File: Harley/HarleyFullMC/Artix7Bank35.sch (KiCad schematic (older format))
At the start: 11 parts, among them U1 xc7a50tcsg324pkg

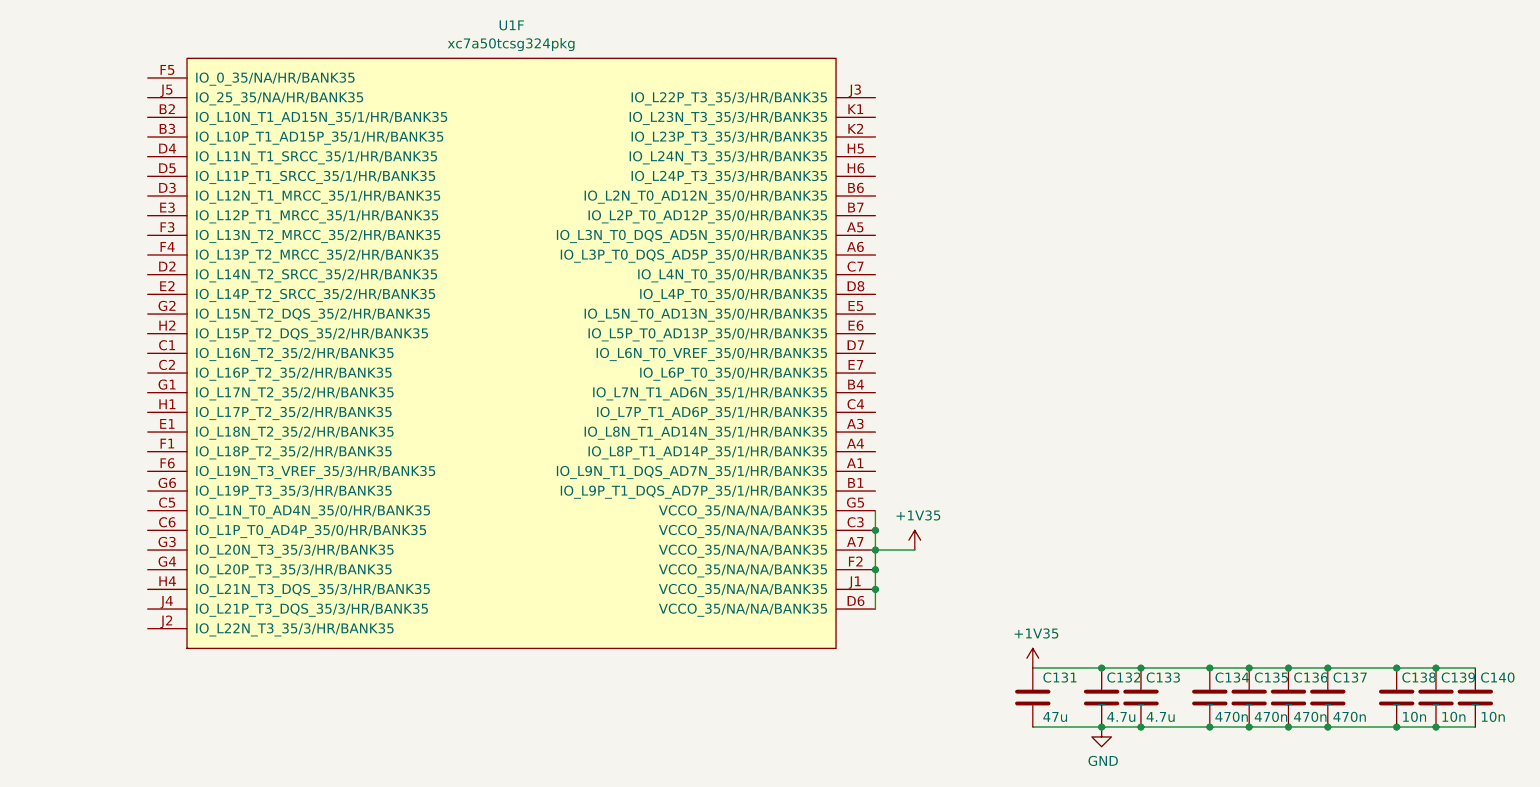
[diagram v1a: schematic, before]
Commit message: finished placement and started routing
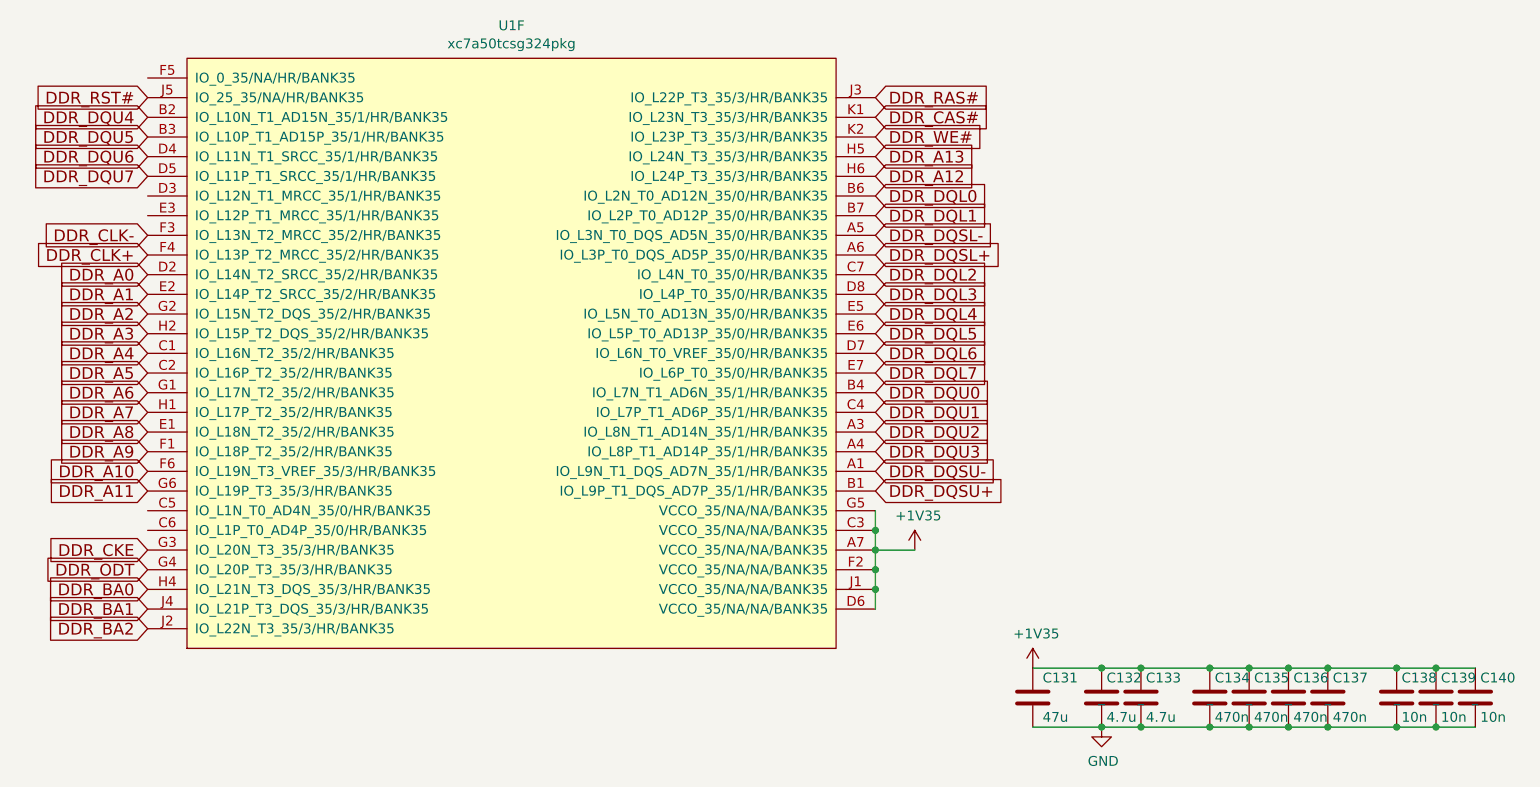
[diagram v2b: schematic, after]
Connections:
- net DDR_DQSU-: now reaches U1.A1 (IO_L9N_T1_DQS_AD7N_35/1/HR/BANK35)
- net DDR_DQU2: now reaches U1.A3 (IO_L8N_T1_AD14N_35/1/HR/BANK35)
- net DDR_DQU3: now reaches U1.A4 (IO_L8P_T1_AD14P_35/1/HR/BANK35)
- net DDR_DQSL-: now reaches U1.A5 (IO_L3N_T0_DQS_AD5N_35/0/HR/BANK35)
- net DDR_DQSL+: now reaches U1.A6 (IO_L3P_T0_DQS_AD5P_35/0/HR/BANK35)
- net DDR_DQSU+: now reaches U1.B1 (IO_L9P_T1_DQS_AD7P_35/1/HR/BANK35)
- net DDR_DQU4: now reaches U1.B2 (IO_L10N_T1_AD15N_35/1/HR/BANK35)
- net DDR_DQU5: now reaches U1.B3 (IO_L10P_T1_AD15P_35/1/HR/BANK35)
- net DDR_DQU0: now reaches U1.B4 (IO_L7N_T1_AD6N_35/1/HR/BANK35)
- net DDR_DQL0: now reaches U1.B6 (IO_L2N_T0_AD12N_35/0/HR/BANK35)
- net DDR_DQL1: now reaches U1.B7 (IO_L2P_T0_AD12P_35/0/HR/BANK35)
- net DDR_A4: now reaches U1.C1 (IO_L16N_T2_35/2/HR/BANK35)
- net DDR_A5: now reaches U1.C2 (IO_L16P_T2_35/2/HR/BANK35)
- net DDR_DQU1: now reaches U1.C4 (IO_L7P_T1_AD6P_35/1/HR/BANK35)
- net DDR_DQL2: now reaches U1.C7 (IO_L4N_T0_35/0/HR/BANK35)
- net DDR_A0: now reaches U1.D2 (IO_L14N_T2_SRCC_35/2/HR/BANK35)
- net DDR_DQU6: now reaches U1.D4 (IO_L11N_T1_SRCC_35/1/HR/BANK35)
- net DDR_DQU7: now reaches U1.D5 (IO_L11P_T1_SRCC_35/1/HR/BANK35)
- net DDR_DQL6: now reaches U1.D7 (IO_L6N_T0_VREF_35/0/HR/BANK35)
- net DDR_DQL3: now reaches U1.D8 (IO_L4P_T0_35/0/HR/BANK35)
- net DDR_A8: now reaches U1.E1 (IO_L18N_T2_35/2/HR/BANK35)
- net DDR_A1: now reaches U1.E2 (IO_L14P_T2_SRCC_35/2/HR/BANK35)
- net DDR_DQL4: now reaches U1.E5 (IO_L5N_T0_AD13N_35/0/HR/BANK35)
- net DDR_DQL5: now reaches U1.E6 (IO_L5P_T0_AD13P_35/0/HR/BANK35)
- net DDR_DQL7: now reaches U1.E7 (IO_L6P_T0_35/0/HR/BANK35)
- net DDR_A9: now reaches U1.F1 (IO_L18P_T2_35/2/HR/BANK35)
- net DDR_CLK-: now reaches U1.F3 (IO_L13N_T2_MRCC_35/2/HR/BANK35)
- net DDR_CLK+: now reaches U1.F4 (IO_L13P_T2_MRCC_35/2/HR/BANK35)
- net DDR_A10: now reaches U1.F6 (IO_L19N_T3_VREF_35/3/HR/BANK35)
- net DDR_A6: now reaches U1.G1 (IO_L17N_T2_35/2/HR/BANK35)
- net DDR_A2: now reaches U1.G2 (IO_L15N_T2_DQS_35/2/HR/BANK35)
- net DDR_CKE: now reaches U1.G3 (IO_L20N_T3_35/3/HR/BANK35)
- net DDR_ODT: now reaches U1.G4 (IO_L20P_T3_35/3/HR/BANK35)
- net DDR_A11: now reaches U1.G6 (IO_L19P_T3_35/3/HR/BANK35)
- net DDR_A7: now reaches U1.H1 (IO_L17P_T2_35/2/HR/BANK35)
- net DDR_A3: now reaches U1.H2 (IO_L15P_T2_DQS_35/2/HR/BANK35)
- net DDR_BA0: now reaches U1.H4 (IO_L21N_T3_DQS_35/3/HR/BANK35)
- net DDR_A13: now reaches U1.H5 (IO_L24N_T3_35/3/HR/BANK35)
- net DDR_A12: now reaches U1.H6 (IO_L24P_T3_35/3/HR/BANK35)
- net DDR_BA2: now reaches U1.J2 (IO_L22N_T3_35/3/HR/BANK35)
- net DDR_RAS#: now reaches U1.J3 (IO_L22P_T3_35/3/HR/BANK35)
- net DDR_BA1: now reaches U1.J4 (IO_L21P_T3_DQS_35/3/HR/BANK35)
- net DDR_RST#: now reaches U1.J5 (IO_25_35/NA/HR/BANK35)
- net DDR_CAS#: now reaches U1.K1 (IO_L23N_T3_35/3/HR/BANK35)
- net DDR_WE#: now reaches U1.K2 (IO_L23P_T3_35/3/HR/BANK35)
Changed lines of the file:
@@
 LIBS:usb3_connector
 LIBS:usb_controller
+LIBS:i2c_flash
 LIBS:power
 LIBS:transistors
@@
 LIBS:contrib
 LIBS:valves
-LIBS:HarleyFullMC-cache
 EELAYER 25 0
 EELAYER END
@@
 Connection ~ 6100 4500
 $Comp
-L GND #PWR74
+L GND #PWR71
 U 1 1 56A272E2
 P 6100 4500
-F 0 "#PWR74" H 6100 4250 50  0001 C CNN
+F 0 "#PWR71" H 6100 4250 50  0001 C CNN
 F 1 "GND" H 6108 4326 50  0000 C CNN
 F 2 "" H 6100 4500 50  0000 C CNN
@@
 Connection ~ 4950 3500
 $Comp
-L +1V35 #PWR52
+L +1V35 #PWR53
 U 1 1 56A288FE
 P 5150 3600
-F 0 "#PWR52" H 5150 3450 50  0001 C CNN
+F 0 "#PWR53" H 5150 3450 50  0001 C CNN
 F 1 "+1V35" H 5168 3774 50  0000 C CNN
 F 2 "" H 5150 3600 50  0000 C CNN
@@
 	5150 3600 4950 3600
 $Comp
-L +1V35 #PWR71
+L +1V35 #PWR69
 U 1 1 56A29C80
 P 5750 4200
-F 0 "#PWR71" H 5750 4050 50  0001 C CNN
+F 0 "#PWR69" H 5750 4050 50  0001 C CNN
 F 1 "+1V35" H 5768 4374 50  0000 C CNN
 F 2 "" H 5750 4200 50  0000 C CNN
@@
 	1    0    0    -1
 $EndComp
+Text GLabel 4950 1800 2    60   Input ~ 0
+DDR_DQL0
+Text GLabel 4950 1900 2    60   Input ~ 0
+DDR_DQL1
+Text GLabel 4950 2200 2    60   Input ~ 0
+DDR_DQL2
+Text GLabel 4950 2300 2    60   Input ~ 0
+DDR_DQL3
+Text GLabel 4950 2400 2    60   Input ~ 0
+DDR_DQL4
+Text GLabel 4950 2500 2    60   Input ~ 0
+DDR_DQL5
+Text GLabel 4950 2600 2    60   Input ~ 0
+DDR_DQL6
+Text GLabel 4950 2700 2    60   Input ~ 0
+DDR_DQL7
+Text GLabel 4950 2800 2    60   Input ~ 0
+DDR_DQU0
+Text GLabel 4950 2900 2    60   Input ~ 0
+DDR_DQU1
+Text GLabel 4950 3000 2    60   Input ~ 0
+DDR_DQU2
+Text GLabel 4950 3100 2    60   Input ~ 0
+DDR_DQU3
+Text GLabel 1250 1400 0    60   Input ~ 0
+DDR_DQU4
+Text GLabel 1250 1500 0    60   Input ~ 0
+DDR_DQU5
+Text GLabel 1250 1600 0    60   Input ~ 0
+DDR_DQU6
+Text GLabel 1250 1700 0    60   Input ~ 0
+DDR_DQU7
+Text GLabel 4950 2100 2    60   Input ~ 0
+DDR_DQSL+
+Text GLabel 4950 2000 2    60   Input ~ 0
+DDR_DQSL-
+Text GLabel 4950 3300 2    60   Input ~ 0
+DDR_DQSU+
+Text GLabel 4950 3200 2    60   Input ~ 0
+DDR_DQSU-
+Text GLabel 1250 2200 0    60   Input ~ 0
+DDR_A0
+Text GLabel 1250 2300 0    60   Input ~ 0
+DDR_A1
+Text GLabel 1250 2400 0    60   Input ~ 0
+DDR_A2
+Text GLabel 1250 2500 0    60   Input ~ 0
+DDR_A3
+Text GLabel 1250 2600 0    60   Input ~ 0
+DDR_A4
+Text GLabel 1250 2700 0    60   Input ~ 0
+DDR_A5
+Text GLabel 1250 2800 0    60   Input ~ 0
+DDR_A6
+Text GLabel 1250 2900 0    60   Input ~ 0
+DDR_A7
+Text GLabel 1250 3000 0    60   Input ~ 0
+DDR_A8
+Text GLabel 1250 3100 0    60   Input ~ 0
+DDR_A9
+Text GLabel 1250 3200 0    60   Input ~ 0
+DDR_A10
+Text GLabel 1250 3300 0    60   Input ~ 0
+DDR_A11
+Text GLabel 4950 1700 2    60   Input ~ 0
+DDR_A12
+Text GLabel 1250 2100 0    60   Input ~ 0
+DDR_CLK+
+Text GLabel 1250 2000 0    60   Input ~ 0
+DDR_CLK-
+Text GLabel 1250 3600 0    60   Input ~ 0
+DDR_CKE
+Text GLabel 4950 1300 2    60   Input ~ 0
+DDR_RAS#
+Text GLabel 4950 1400 2    60   Input ~ 0
+DDR_CAS#
+Text GLabel 4950 1500 2    60   Input ~ 0
+DDR_WE#
+Text GLabel 1250 3800 0    60   Input ~ 0
+DDR_BA0
+Text GLabel 1250 3900 0    60   Input ~ 0
+DDR_BA1
+Text GLabel 1250 4000 0    60   Input ~ 0
+DDR_BA2
+Text GLabel 1250 3700 0    60   Input ~ 0
+DDR_ODT
+Text GLabel 4950 1600 2    60   Input ~ 0
+DDR_A13
+Text GLabel 1250 1300 0    60   Input ~ 0
+DDR_RST#
 $EndSCHEMATC

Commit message: first routing
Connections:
- net DDR_A0: now also U1.G2 (IO_L15N_T2_DQS_35/2/HR/BANK35); no longer U1.D2 (IO_L14N_T2_SRCC_35/2/HR/BANK35)
- net DDR_A1: now also U1.H5 (IO_L24N_T3_35/3/HR/BANK35); no longer U1.E2 (IO_L14P_T2_SRCC_35/2/HR/BANK35)
- net DDR_A11: now also U1.H4 (IO_L21N_T3_DQS_35/3/HR/BANK35); no longer U1.G6 (IO_L19P_T3_35/3/HR/BANK35)
- net DDR_A12: now also U1.G4 (IO_L20P_T3_35/3/HR/BANK35); no longer U1.H6 (IO_L24P_T3_35/3/HR/BANK35)
- net DDR_A13: now also U1.K2 (IO_L23P_T3_35/3/HR/BANK35); no longer U1.H5 (IO_L24N_T3_35/3/HR/BANK35)
- net DDR_A2: now also U1.G3 (IO_L20N_T3_35/3/HR/BANK35); no longer U1.G2 (IO_L15N_T2_DQS_35/2/HR/BANK35)
- net DDR_A4: now also U1.J4 (IO_L21P_T3_DQS_35/3/HR/BANK35); no longer U1.C1 (IO_L16N_T2_35/2/HR/BANK35)
- net DDR_A5: now also U1.J2 (IO_L22N_T3_35/3/HR/BANK35); no longer U1.C2 (IO_L16P_T2_35/2/HR/BANK35)
- net DDR_A6: now also U1.G6 (IO_L19P_T3_35/3/HR/BANK35); no longer U1.G1 (IO_L17N_T2_35/2/HR/BANK35)
- net DDR_A7: now also U1.K1 (IO_L23N_T3_35/3/HR/BANK35); no longer U1.H1 (IO_L17P_T2_35/2/HR/BANK35)
- net DDR_A8: now also U1.H6 (IO_L24P_T3_35/3/HR/BANK35); no longer U1.E1 (IO_L18N_T2_35/2/HR/BANK35)
- net DDR_A9: now also U1.J3 (IO_L22P_T3_35/3/HR/BANK35); no longer U1.F1 (IO_L18P_T2_35/2/HR/BANK35)
- net DDR_BA0: now also U1.E1 (IO_L18N_T2_35/2/HR/BANK35); no longer U1.H4 (IO_L21N_T3_DQS_35/3/HR/BANK35)
- net DDR_BA1: now also U1.G1 (IO_L17N_T2_35/2/HR/BANK35); no longer U1.J4 (IO_L21P_T3_DQS_35/3/HR/BANK35)
- net DDR_BA2: now also U1.F1 (IO_L18P_T2_35/2/HR/BANK35); no longer U1.J2 (IO_L22N_T3_35/3/HR/BANK35)
- net DDR_CAS#: now also U1.C1 (IO_L16N_T2_35/2/HR/BANK35); no longer U1.K1 (IO_L23N_T3_35/3/HR/BANK35)
- net DDR_CKE: now also U1.H1 (IO_L17P_T2_35/2/HR/BANK35); no longer U1.G3 (IO_L20N_T3_35/3/HR/BANK35)
- net DDR_DQL0: now also U1.B7 (IO_L2P_T0_AD12P_35/0/HR/BANK35); no longer U1.B6 (IO_L2N_T0_AD12N_35/0/HR/BANK35)
- net DDR_DQL1: now also U1.D8 (IO_L4P_T0_35/0/HR/BANK35); no longer U1.B7 (IO_L2P_T0_AD12P_35/0/HR/BANK35)
- net DDR_DQL3: now also U1.B6 (IO_L2N_T0_AD12N_35/0/HR/BANK35); no longer U1.D8 (IO_L4P_T0_35/0/HR/BANK35)
- net DDR_DQL5: now also U1.D7 (IO_L6N_T0_VREF_35/0/HR/BANK35); no longer U1.E6 (IO_L5P_T0_AD13P_35/0/HR/BANK35)
- net DDR_DQL6: now also U1.E6 (IO_L5P_T0_AD13P_35/0/HR/BANK35); no longer U1.D7 (IO_L6N_T0_VREF_35/0/HR/BANK35)
- net DDR_DQU0: now also U1.B2 (IO_L10N_T1_AD15N_35/1/HR/BANK35); no longer U1.B4 (IO_L7N_T1_AD6N_35/1/HR/BANK35)
- net DDR_DQU1: now also U1.D4 (IO_L11N_T1_SRCC_35/1/HR/BANK35); no longer U1.C4 (IO_L7P_T1_AD6P_35/1/HR/BANK35)
- net DDR_DQU2: now also U1.B3 (IO_L10P_T1_AD15P_35/1/HR/BANK35); no longer U1.A3 (IO_L8N_T1_AD14N_35/1/HR/BANK35)
- net DDR_DQU3: now also U1.D5 (IO_L11P_T1_SRCC_35/1/HR/BANK35); no longer U1.A4 (IO_L8P_T1_AD14P_35/1/HR/BANK35)
- net DDR_DQU4: now also U1.B4 (IO_L7N_T1_AD6N_35/1/HR/BANK35); no longer U1.B2 (IO_L10N_T1_AD15N_35/1/HR/BANK35)
- net DDR_DQU5: now also U1.C4 (IO_L7P_T1_AD6P_35/1/HR/BANK35); no longer U1.B3 (IO_L10P_T1_AD15P_35/1/HR/BANK35)
- net DDR_DQU6: now also U1.A3 (IO_L8N_T1_AD14N_35/1/HR/BANK35); no longer U1.D4 (IO_L11N_T1_SRCC_35/1/HR/BANK35)
- net DDR_DQU7: now also U1.A4 (IO_L8P_T1_AD14P_35/1/HR/BANK35); no longer U1.D5 (IO_L11P_T1_SRCC_35/1/HR/BANK35)
- net DDR_ODT: now also U1.E2 (IO_L14P_T2_SRCC_35/2/HR/BANK35); no longer U1.G4 (IO_L20P_T3_35/3/HR/BANK35)
- net DDR_RAS#: now also U1.C2 (IO_L16P_T2_35/2/HR/BANK35); no longer U1.J3 (IO_L22P_T3_35/3/HR/BANK35)
- net DDR_WE#: now also U1.D2 (IO_L14N_T2_SRCC_35/2/HR/BANK35); no longer U1.K2 (IO_L23P_T3_35/3/HR/BANK35)
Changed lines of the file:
@@
 LIBS:contrib
 LIBS:valves
+LIBS:HarleyFullMC-cache
 EELAYER 25 0
 EELAYER END
@@
 	1    0    0    -1
 $EndComp
-Text GLabel 4950 1800 2    60   Input ~ 0
+Text GLabel 4950 1900 2    60   Input ~ 0
 DDR_DQL0
-Text GLabel 4950 1900 2    60   Input ~ 0
+Text GLabel 4950 2300 2    60   Input ~ 0
 DDR_DQL1
 Text GLabel 4950 2200 2    60   Input ~ 0
 DDR_DQL2
-Text GLabel 4950 2300 2    60   Input ~ 0
+Text GLabel 4950 1800 2    60   Input ~ 0
 DDR_DQL3
 Text GLabel 4950 2400 2    60   Input ~ 0
 DDR_DQL4
+Text GLabel 4950 2600 2    60   Input ~ 0
+DDR_DQL5
 Text GLabel 4950 2500 2    60   Input ~ 0
-DDR_DQL5
-Text GLabel 4950 2600 2    60   Input ~ 0
 DDR_DQL6
 Text GLabel 4950 2700 2    60   Input ~ 0
 DDR_DQL7
+Text GLabel 1250 1400 0    60   Input ~ 0
+DDR_DQU0
+Text GLabel 1250 1600 0    60   Input ~ 0
+DDR_DQU1
+Text GLabel 1250 1500 0    60   Input ~ 0
+DDR_DQU2
+Text GLabel 1250 1700 0    60   Input ~ 0
+DDR_DQU3
 Text GLabel 4950 2800 2    60   Input ~ 0
-DDR_DQU0
+DDR_DQU4
 Text GLabel 4950 2900 2    60   Input ~ 0
-DDR_DQU1
+DDR_DQU5
 Text GLabel 4950 3000 2    60   Input ~ 0
-DDR_DQU2
+DDR_DQU6
 Text GLabel 4950 3100 2    60   Input ~ 0
-DDR_DQU3
-Text GLabel 1250 1400 0    60   Input ~ 0
-DDR_DQU4
-Text GLabel 1250 1500 0    60   Input ~ 0
-DDR_DQU5
-Text GLabel 1250 1600 0    60   Input ~ 0
-DDR_DQU6
-Text GLabel 1250 1700 0    60   Input ~ 0
 DDR_DQU7
 Text GLabel 4950 2100 2    60   Input ~ 0
@@
 Text GLabel 4950 3200 2    60   Input ~ 0
 DDR_DQSU-
-Text GLabel 1250 2200 0    60   Input ~ 0
+Text GLabel 1250 2400 0    60   Input ~ 0
 DDR_A0
-Text GLabel 1250 2300 0    60   Input ~ 0
+Text GLabel 4950 1600 2    60   Input ~ 0
 DDR_A1
-Text GLabel 1250 2400 0    60   Input ~ 0
+Text GLabel 1250 3600 0    60   Input ~ 0
 DDR_A2
 Text GLabel 1250 2500 0    60   Input ~ 0
 DDR_A3
-Text GLabel 1250 2600 0    60   Input ~ 0
+Text GLabel 1250 3900 0    60   Input ~ 0
 DDR_A4
-Text GLabel 1250 2700 0    60   Input ~ 0
+Text GLabel 1250 4000 0    60   Input ~ 0
 DDR_A5
-Text GLabel 1250 2800 0    60   Input ~ 0
+Text GLabel 1250 3300 0    60   Input ~ 0
 DDR_A6
-Text GLabel 1250 2900 0    60   Input ~ 0
+Text GLabel 4950 1400 2    60   Input ~ 0
 DDR_A7
-Text GLabel 1250 3000 0    60   Input ~ 0
+Text GLabel 4950 1700 2    60   Input ~ 0
 DDR_A8
-Text GLabel 1250 3100 0    60   Input ~ 0
+Text GLabel 4950 1300 2    60   Input ~ 0
 DDR_A9
 Text GLabel 1250 3200 0    60   Input ~ 0
 DDR_A10
-Text GLabel 1250 3300 0    60   Input ~ 0
+Text GLabel 1250 3800 0    60   Input ~ 0
 DDR_A11
-Text GLabel 4950 1700 2    60   Input ~ 0
+Text GLabel 1250 3700 0    60   Input ~ 0
 DDR_A12
 Text GLabel 1250 2100 0    60   Input ~ 0
@@
 Text GLabel 1250 2000 0    60   Input ~ 0
 DDR_CLK-
-Text GLabel 1250 3600 0    60   Input ~ 0
+Text GLabel 1250 2900 0    60   Input ~ 0
 DDR_CKE
-Text GLabel 4950 1300 2    60   Input ~ 0
+Text GLabel 1250 2700 0    60   Input ~ 0
 DDR_RAS#
-Text GLabel 4950 1400 2    60   Input ~ 0
+Text GLabel 1250 2600 0    60   Input ~ 0
 DDR_CAS#
+Text GLabel 1250 2200 0    60   Input ~ 0
+DDR_WE#
+Text GLabel 1250 3000 0    60   Input ~ 0
+DDR_BA0
+Text GLabel 1250 2800 0    60   Input ~ 0
+DDR_BA1
+Text GLabel 1250 3100 0    60   Input ~ 0
+DDR_BA2
+Text GLabel 1250 2300 0    60   Input ~ 0
+DDR_ODT
 Text GLabel 4950 1500 2    60   Input ~ 0
-DDR_WE#
-Text GLabel 1250 3800 0    60   Input ~ 0
-DDR_BA0
-Text GLabel 1250 3900 0    60   Input ~ 0
-DDR_BA1
-Text GLabel 1250 4000 0    60   Input ~ 0
-DDR_BA2
-Text GLabel 1250 3700 0    60   Input ~ 0
-DDR_ODT
-Text GLabel 4950 1600 2    60   Input ~ 0
 DDR_A13
 Text GLabel 1250 1300 0    60   Input ~ 0

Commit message: generate BOM and update all components accordingly
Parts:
- C131: D1PL _ -> http://www.digikey.com/product-detail/en/C2012X5R1A476M125A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; D1PN _ -> 445-8239; MFN _ -> TDK; MFP _ -> C2012X5R1A476M125AC; Package 0402 -> 0805; Tolerance 10% -> 20%; Voltage 6.3 -> 10
- C132, C133: D2 mouser -> avnet; D2PL _ -> http://avnetexpress.avnet.com/store/em/EMController?action=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; D2PN _ -> C1005X5R0J475K050BC/BKN
- U1: D1 digikey -> avnet; D1PL _ -> http://avnetexpress.avnet.com/store/em/EMController?action=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; D1PN _ -> XC7A50T-2CSG324C; D2 mouser -> _; MFN _ -> Xilinx; MFP _ -> XC7A50T-2CSG324C

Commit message: updated part number for available components and generated archive for quote
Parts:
- U1: value xc7a50tcsg324pkg -> xc7a100tcsg324pkg; symbol xc7a50tcsg324pkg -> xc7a100tcsg324pkg; D1 avnet -> digikey; D1PL http://avnetexpress.avnet.com/store/em/EMController?action=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 -> http://www.digikey.com/product-detail/en/XC7A100T-2CSG324I/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; D1PN XC7A50T-2CSG324C -> 122-1881; MFP XC7A50T-2CSG324C -> XC7A100T-2CSG324I
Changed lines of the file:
@@
 $EndDescr
 $Comp
-L xc7a50tcsg324pkg U1
+L xc7a100tcsg324pkg U1
 U 6 1 56A04FF9
 P 3150 2600
 F 0 "U1" H 3100 4266 50  0000 C CNN
-F 1 "xc7a50tcsg324pkg" H 3100 4174 50  0000 C CNN
+F 1 "xc7a100tcsg324pkg" H 3100 4174 50  0000 C CNN
 F 2 "BGA:BGA324C80P18X18_1500X1500X150" H 3150 2600 50  0001 C CNN
 F 3 "http://www.xilinx.com/support/documentation/data_sheets/ds180_7Series_Overview.pdf" H 3150 2600 50  0001 C CNN
 F 4 "Xilinx" H 3150 2600 50  0001 C CNN "MFN"
-F 5 "XC7A50T-2CSG324C" H 3150 2600 50  0001 C CNN "MFP"
-F 6 "avnet" H 3150 2600 50  0001 C CNN "D1"
+F 5 "XC7A100T-2CSG324I" H 3150 2600 50  0001 C CNN "MFP"
+F 6 "digikey" H 3150 2600 50  0001 C CNN "D1"
 F 7 "_" H 3150 2600 50  0001 C CNN "D2"
-F 8 "XC7A50T-2CSG324C" H 3150 2600 50  0001 C CNN "D1PN"
-F 9 "http://avnetexpress.avnet.com/store/em/EMController?action=products&catalogId=500201&storeId=500201&N=0&defaultCurrency=USD&langId=-1&slnk=e&term=XC7A50T-2CSG324C&mfr=XLX&CMP=KNC-Octopart_VSE&c=USD&l=-1" H 3150 2600 50  0001 C CNN "D1PL"
+F 8 "122-1881" H 3150 2600 50  0001 C CNN "D1PN"
+F 9 "http://www.digikey.com/product-detail/en/XC7A100T-2CSG324I/122-1881-ND/3925808" H 3150 2600 50  0001 C CNN "D1PL"
 F 10 "_" H 3150 2600 50  0001 C CNN "D2PN"
 F 11 "_" H 3150 2600 50  0001 C CNN "D2PL"
